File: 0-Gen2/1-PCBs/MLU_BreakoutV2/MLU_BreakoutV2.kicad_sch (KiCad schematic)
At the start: 41 parts, among them J1 Conn_02x24_Odd_Even, J10 Conn_01x17_Pin, J11 430450228, J12 430450228, J13 430450228, J14 430450228, J15 430450228, J16 430450228, J2 Conn_01x03_Pin, J21 430450228, J22 430450228, J3 PixHawk PM02, J4 BUS1, J5 BUS2, J6 Conn_01x02_Pin, J7 Conn_02x02_Odd_Even, J8 UART, J9 Conn_01x09_Pin, U1 MCP23008-E_P, U2 MCP9808_MSOP, U3 BME280, U4 Teensy4.1, U5 MCP9808_MSOP

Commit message: [add] MLU2 progress, [bugfix] depth sensor
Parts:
- removed J12, J13, J14, J15, J16, J21, J22: 430450228, ImportedV2:CONN_SD-43045-010_02_MOL, symbol Imported:430450228
- removed J6: Conn_01x02_Pin, Connector_PinHeader_2.54mm:PinHeader_1x02_P2.54mm_Vertical, symbol Connector:Conn_01x02_Pin
- removed J7: Conn_02x02_Odd_Even, Connector_PinHeader_2.54mm:PinHeader_2x02_P2.54mm_Vertical, symbol Connector_Generic:Conn_02x02_Odd_Even
- removed J9: Conn_01x09_Pin, Connector_PinHeader_2.54mm:PinHeader_1x09_P2.54mm_Vertical, symbol Connector:Conn_01x09_Pin
- removed JP1, JP2: Jumper_3_Bridged12, Jumper:SolderJumper-3_P1.3mm_Bridged2Bar12_RoundedPad1.0x1.5mm, symbol Jumper:Jumper_3_Bridged12
- added C5: 10uF, Capacitor_SMD:C_0805_2012Metric_Pad1.18x1.45mm_HandSolder, symbol Device:C
- added C6: 0.1uF, ImportedV2:K104K15X7RF5TL2_VIS, symbol Device:C
- added D1, D2: LED, LED_THT:LED_D3.0mm, symbol Device:LED
- added D3: 1N5817, Diode_THT:D_5W_P12.70mm_Horizontal, symbol Device:D
- added H10: Molex Socket Crimps, symbol Mechanical:MountingHole
- added H11, H8: Molex 4 Pin Male, symbol Mechanical:MountingHole
- added H12: MountingHole, MountingHole:MountingHole_3.2mm_M3, symbol Mechanical:MountingHole
- added H2, H5: IDC Cable, symbol Mechanical:MountingHole
- added H6: Socket for Teensy, symbol Mechanical:MountingHole
- added H7: Molex 10 Pin Male, symbol Mechanical:MountingHole
- added H9: Molex 2 Pin Male, symbol Mechanical:MountingHole
- added J12: J1B1211CCD, ImportedV2:J1B1211CCD, symbol Imported:J1B1211CCD
- added J13: Conn_02x03_Odd_Even, Connector_PinHeader_2.00mm:PinHeader_2x03_P2.00mm_Vertical, symbol Connector_Generic:Conn_02x03_Odd_Even
- added J14: 430451027, ImportedV2:CONN_SD-43045-010_10_MOL, symbol Imported:430451027
- added J17, J18, J19, J20, J23, J24: 430450228, ImportedV2:CONN_SD-43045-001_02_MOL, symbol Imported:430450228
- added J25, J7: SBH11-PBPC-D10-ST-BK, ImportedV2:SULLINS_SBH11-PBPC-D10-ST-BK, symbol Imported_Symbols:SBH11-PBPC-D10-ST-BK
- added J26: 430450422, ImportedV2:CONN_SD-43045-008_04_MOL, symbol Imported:430450422
- added J6, J9: 430450422, ImportedV2:CONN_SD-43045-009_04_MOL, symbol Imported:430450422
- added R8, R9: 140, Resistor_SMD:R_0805_2012Metric_Pad1.20x1.40mm_HandSolder, symbol Device:R_US
- added SW1: 09.03201.02, ImportedV2:09.03201_EAO, symbol Imported_Symbols:09.03201.02
- added U6: Teensy4.1, Module:Teensy41, symbol teensy:Teensy4.1
- added U8: BA033CC0FP-E2, ImportedV2:TO252-3_ROM, symbol Imported:BA033CC0FP-E2
- U3: footprint Imported Footprints:BME280 -> ImportedV2:BME280
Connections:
- net +3.3V: now also J19.2, J20.2, J25.18, J26.1, J7.18, U8.3 (OUT); no longer J1.11 (Pin_11), J1.15 (Pin_15), J1.23 (Pin_23)
- net +5V: now also J14.1, J17.1, J25.14, J25.16, J7.14, J7.16, J9.1, SW1.1, U8.1 (Vcc)
- net D5: now also J14.4
- net D6: now also J14.5
- net D7: now also J14.8
- net Dleak: now also U6.25 (33_MCLK2)
- net Dled1: now also J23.1, U6.29 (37_CS); no longer J1.3 (Pin_3)
- net Dled2: now also J24.1, U6.28 (36_CS); no longer J1.7 (Pin_7)
- net Dswitch1: now also J19.1, U6.18 (26_A12_MOSI1); no longer J1.9 (Pin_9)
- net Dswitch2: now also J20.1, J25.8, U6.19 (27_A13_SCK1); no longer J1.13 (Pin_13)
- net GND: now also C5.2, C6.1, J12.8 (GND), J12.9, J13.4 (Pin_4), J14.2, J18.2, J23.2, J24.2, J25.12, J25.20, J26.4, J7.12, J7.20, J9.4, R8.2, R9.2, U6.1 (GND), U6.34 (GND), U6.47 (GND), U6.64 (GND), U8.2 (GND); no longer J1.1 (Pin_1), J1.17 (Pin_17), J1.37 (Pin_37), J1.43 (Pin_43), J1.5 (Pin_5), J11.2
- net I2C1_SCL: now also J25.2, J26.3, J7.2, U6.41 (19_A5_SCL)
- net I2C1_SDA: now also J25.4, J26.2, J7.4, U6.40 (18_A4_SDA)
- net PWM0: now also J7.1, U6.2 (0_RX1_CRX2_CS1); no longer J11.1
- net PWM1: now also J7.3, U6.3 (1_TX1_CTX2_MISO1)
- net PWM2: now also J7.5, U6.4 (2_OUT2)
- net PWM3: now also J7.7, U6.5 (3_LRCLK2)
- net PWM4: now also J7.9, U6.6 (4_BCLK2)
- net PWM5: now also J7.11, U6.7 (5_IN2)
- net PWM6: now also J7.13, U6.8 (6_OUT1D)
- net PWM7: now also J7.15, U6.9 (7_RX2_OUT1A)
- net PWM8: no longer J1.47 (Pin_47)
- net SPI_CS1: now also J14.3
- net SPI_MISO: now also J14.9
- net SPI_MOSI: now also J14.6
- net SPI_SCK: now also J14.7
- net PWM9: no longer names the net of J1.41 (Pin_41)
- new net: C5.1, D2.2 (A), D3.2 (A), J17.2, SW1.3
- new net: C6.2, J12.2, J12.5
- new net: D1.2 (A), SW1.2
- new net: D1.1 (K), R8.1
- new net: D2.1 (K), R9.1
- new net LED: J12.10, J13.3 (Pin_3), U6.61 (LED)
- new net Lumen_PWM: J18.1, U6.10 (8_TX2_IN1)
- new net R+: J12.4, J13.1 (Pin_1), U6.60 (R+)
- new net R-: J12.6, J13.2 (Pin_2), U6.65 (R-)
- new net T+: J12.1, J13.6 (Pin_6), U6.63 (T+)
- new net T-: J12.3, J13.5 (Pin_5), U6.62 (T-)
- new net Teensy_5V: D3.1 (K), U6.48 (VIN)
- new net outNEO_CTRL_ESCs: J9.2
- new net outNEO_CTRL_ESCs_M: J7.8
- new net outNEO_CTRL_ESCs_S: J7.19
- new net toNEO_CTRL_ESCs_M: J7.6, U6.11 (9_OUT1C)
- new net toNEO_CTRL_ESCs_S: J7.17, U6.12 (10_CS_MQSR)
- new net toNEO_CTRL_EXTs: J9.3, U6.13 (11_MOSI_CTX1)
- no-connect marks 24 -> 44
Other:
- added sheet NEOs (NEOs.kicad_sch)
- note added: "-Route with diff pairs -Avoid vias"
- note added: "3.3V, 1A output"
- note added: "5V --> 3.3V Reg"
- note added: "Attach jumper when running off of 12V supply. Remove jumper when programming. -Expect 600mA draw"
- note added: "BlueRobotics Depth Sensor I2C @ 0x76"
- note added: "Bulkhead LEDs"
- note added: "Data Log Switch"
- note added: "Ethernet Breakout"
- note added: "Hardware/Software Kill Switch"
- note added: "Interconnect to ESC Board"
- note added: "Interconnect to Orin"
- note added: "Lumen LED PWM"
- note added: "Make sure to cut the 5V trace (or add diode): https://www.pjrc.com/teensy/external_power.html"
- note added: "More info: https://oshpark.com/shared_projects/wUFt1emZ https://www.pjrc.com/store/ethernet_kit.html"
- note added: "Neo_Interface_Exts"
- note added: "Neos"
- note added: "TODO: neopixel lines to power dist board Fix the screen pins"
- note added: "Teensy Reset Switch (Internal and External)"
- note added: "This is passed to Orin board"
- note added: "To external BlueRobotics switch on bulkhead"
- note added: "Vertical Mount"
- note added: "Vf=~2.2V, 20mA. Make this Green"
- note added: "Vf=~2.2V, 20mA. Make this Red"
- note added: "don't change pinout here"
- note added: "pick whether to chain from ESC board or have on new pin"
- note added: "socket here + leave space to mount"
- note removed: "0x76"
- note removed: "Bulkhead Interface"
- note removed: "Depth Sensor"
- note removed: "LEDs"
- note removed: "Lights Daisy Chain"
- note removed: "Note: light power supply must come from unregulated high voltage line"
- note removed: "Orin Passthrough"
- note removed: "Peripheral Interfaces"
- note removed: "Power Distrbution Interface"
- note removed: "Thruster Interface"
- note removed: "Towards the bulkhead"
- note removed: "likely move these to the ESC board"
- moved on the sheet: C1, C2, C3, J3, J8, JP3, R6, R7, RN1A, RN1B, RN1C, RN1D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

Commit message: [bugfix] depth via BME 0x76 removal, [add] MLUv2 progress
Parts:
- removed C1, C2: 135p, Capacitor_SMD:C_0603_1608Metric_Pad1.08x0.95mm_HandSolder, symbol Device:C
- removed C3, C4: 10uF, Capacitor_SMD:C_0805_2012Metric_Pad1.18x1.45mm_HandSolder, symbol Device:C
- removed H8: Molex 4 Pin Male, symbol Mechanical:MountingHole
- removed J1: Conn_02x24_Odd_Even, Connector_PinSocket_2.54mm:PinSocket_2x24_P2.54mm_Horizontal, symbol Connector_Generic:Conn_02x24_Odd_Even
- removed J18, J19, J20, J23, J24: 430450228, ImportedV2:CONN_SD-43045-001_02_MOL, symbol Imported:430450228
- removed J2: Conn_01x03_Pin, Connector_PinHeader_2.54mm:PinHeader_1x03_P2.54mm_Vertical, symbol Connector:Conn_01x03_Pin
- removed J26: 430450422, ImportedV2:CONN_SD-43045-008_04_MOL, symbol Imported:430450422
- removed J4: BUS1, Connector_PinSocket_2.54mm:PinSocket_1x04_P2.54mm_Vertical, symbol Connector:Conn_01x04_Pin
- removed J5: BUS2, Connector_PinSocket_2.54mm:PinSocket_1x04_P2.54mm_Vertical, symbol Connector:Conn_01x04_Pin
- removed JP3: Jumper_3_Bridged12, Jumper:SolderJumper-3_P1.3mm_Bridged2Bar12_RoundedPad1.0x1.5mm, symbol Jumper:Jumper_3_Bridged12
- removed R1, R2, R3, R6, R7: 10k, Resistor_SMD:R_0805_2012Metric_Pad1.20x1.40mm_HandSolder, symbol Device:R_US
- removed RN1: 10kΩ, Resistor_SMD:R_Array_Convex_4x0612, symbol Lab_3:R_Pack04_Split
- removed U1: MCP23008-E_P, Imported Footprints:MCP3008, symbol Imported:MCP23008-E_P
- removed U2, U5: MCP9808_MSOP, Package_SO:MSOP-8_3x3mm_P0.65mm, symbol Sensor_Temperature:MCP9808_MSOP
- removed U3: BME280, ImportedV2:BME280, symbol Sensor:BME280
- added J8: Conn_02x20_Odd_Even, Connector_PinSocket_2.54mm:PinSocket_2x20_P2.54mm_Vertical, symbol Connector_Generic:Conn_02x20_Odd_Even
- added JP4, JP7: Jumper_2_Small_Open, Jumper:SolderJumper-2_P1.3mm_Open_RoundedPad1.0x1.5mm, symbol Jumper:Jumper_2_Small_Open
- added JP5, JP6: Jumper_2_Small_Bridged, Jumper:SolderJumper-2_P1.3mm_Bridged2Bar_RoundedPad1.0x1.5mm, symbol Jumper:Jumper_2_Small_Bridged
- renumbered C5 to C1, C6 to C2, D3 to D1, D1 to D2, D2 to D3, H11 to H1, H3 to H10, H4 to H11, H7 to H2, H9 to H3, H10 to H4, H2 to H5, H5 to H7, H1 to H8, H12 to H9, J12 to J10, J13 to J11, J3 to J12, J25 to J13, J6 to J14, J11 to J15, J8 to J16, J9 to J4, J14 to J5, J17 to J6, J10 to J9, R8 to R6, R9 to R7, U4 to U1, U8 to U5
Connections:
- net +3.3V: now also J13.7, J8.19 (Pin_19), J8.3 (Pin_3); no longer J13.18, U1.15 (3V3), U1.46 (3V3)
- net +5V: now also J13.1, J13.3, J13.5, J4.4, J8.1 (Pin_1), J8.17 (Pin_17); no longer J13.14, J13.16, J4.1, U1.48 (VIN)
- net Ab_s: no longer U1.44 (22_A8_CTX1)
- net Ai_s: no longer U1.45 (23_A9_CRX1_MCLK1)
- net Analog_Current: now also U6.33 (41_A17), JP4.1 (A), JP5.2 (B); no longer U1.33 (41_A17)
- net Analog_Voltage: now also U6.32 (40_A16), JP6.2 (B), JP7.2 (B); no longer U1.32 (40_A16)
- net D5: no longer U1.36 (14_A0_TX3_SPDIF_OUT)
- net Dleak: no longer U1.25 (33_MCLK2)
- net Dled1: no longer U1.29 (37_CS)
- net Dled2: no longer U1.28 (36_CS)
- net Dswitch1: no longer U1.18 (26_A12_MOSI1)
- net Dswitch2: now also J13.6; no longer J13.8, U1.19 (27_A13_SCK1)
- net GND: now also J13.13, J13.15, J13.17, J13.19, J4.2, J8.18 (Pin_18), J8.2 (Pin_2), J8.20 (Pin_20), J8.34 (Pin_34), J8.36 (Pin_36), J8.4 (Pin_4), JP4.2 (B), JP7.1 (A); no longer J13.12, J13.20, J4.4, U1.1 (GND), U1.34 (GND), U1.47 (GND)
- net I2C1_SCL: now also J8.7 (Pin_7); no longer U1.41 (19_A5_SCL)
- net I2C1_SDA: now also J8.5 (Pin_5); no longer U1.40 (18_A4_SDA)
- net I2C2_SCL: now also U6.38 (16_A2_RX4_SCL1), J8.8 (Pin_8); no longer U1.38 (16_A2_RX4_SCL1)
- net I2C2_SDA: now also U6.39 (17_A3_TX4_SDA1), J8.6 (Pin_6); no longer U1.39 (17_A3_TX4_SDA1)
- net PWM0: no longer U1.2 (0_RX1_CRX2_CS1)
- net PWM1: no longer U1.3 (1_TX1_CTX2_MISO1)
- net PWM2: no longer U1.4 (2_OUT2)
- net PWM3: no longer U1.5 (3_LRCLK2)
- net PWM4: no longer U1.6 (4_BCLK2)
- net PWM5: no longer U1.7 (5_IN2)
- net PWM6: no longer U1.8 (6_OUT1D)
- net PWM7: no longer U1.9 (7_RX2_OUT1A)
- net SPI_CS1: now also U6.12 (10_CS_MQSR); no longer U1.12 (10_CS_MQSR)
- net SPI_MISO: now also U6.14 (12_MISO_MQSL); no longer U1.14 (12_MISO_MQSL)
- net SPI_MOSI: now also U6.13 (11_MOSI_CTX1); no longer U1.13 (11_MOSI_CTX1)
- net SPI_SCK: now also U6.35 (13_SCK_LED); no longer U1.35 (13_SCK_LED)
- net UART_RX2: now also U6.20 (28_RX7), J8.26 (Pin_26); no longer U1.20 (28_RX7)
- net UART_RX3: now also U6.17 (25_A11_RX6_SDA2), J8.30 (Pin_30)
- net UART_TX2: now also U6.21 (29_TX7), J8.28 (Pin_28); no longer U1.21 (29_TX7)
- net UART_TX3: now also U6.16 (24_A10_TX6_SCL2), J8.32 (Pin_32)
- net outNEO_CTRL_ESCs: now also J4.1; no longer J4.2
- net toNEO_CTRL_ESCs_M: no longer U6.11 (9_OUT1C)
- net toNEO_CTRL_ESCs_S: no longer U6.12 (10_CS_MQSR)
- net toNEO_CTRL_EXTs: no longer U6.13 (11_MOSI_CTX1)
- net D/A14: now reaches U6.36 (14_A0_TX3_SPDIF_OUT)
- net D/A14: now also J8.10 (Pin_10)
- net GPIOExp_INT: now reaches U6.37 (15_A1_RX3_SPDIF_IN)
- net D/A20: now reaches U6.42 (20_A6_TX5_LRCLK1)
- net D/A20: now also J8.9 (Pin_9)
- net D/A21: now reaches U6.43 (21_A7_RX5_BCLK1)
- net D/A21: now also J8.11 (Pin_11)
- net D/A22: now reaches U6.44 (22_A8_CTX1)
- net D/A22: now also J8.13 (Pin_13)
- net D/A23: now reaches U6.45 (23_A9_CRX1_MCLK1)
- net D/A23: now also J8.15 (Pin_15)
- net Host_D-: now reaches U6.56 (D-)
- net Host_D-: now also J8.21 (Pin_21)
- net Host_D+: now reaches U6.57 (D+)
- net Host_D+: now also J8.23 (Pin_23)
- net at J13.10: now also JP6.1 (A)
- net A3: no longer names the net of U1.43 (21_A7_RX5_BCLK1)
- net A4: no longer names the net of U1.42 (20_A6_TX5_LRCLK1)
- net Dint: no longer names the net of U1.37 (15_A1_RX3_SPDIF_IN)
- net PWM8: no longer names the net of U1.10 (8_TX2_IN1)
- new net: J13.8, JP5.1 (A)
- no-connect marks 44 -> 38
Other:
- sheet NEOs renamed Neopixels
- added sheet GPIO_Expander (GPIO_Expander.kicad_sch)
- added sheet On-board Sensors (sensors.kicad_sch)
- added sheet Peripheral Connectors (peripherals.kicad_sch)
- sheet Neopixels ports: added outNEO_MLU, toNEO_MLU; removed none
- note added: "5V Orin-->MLU 3.3V MLU-->Orin"
- note added: "Arm Host"
- note added: "Extra Pin Breakout"
- note added: "Interrupt to GPIO Expander"
- note added: "Secondary I2C Bus"
- note added: "Solder resistors onto jumpers if voltage division is necessary"
- note added: "TODO: neopixel lines to power dist board fix the screen pins subset LEDs on MLU arm connector XT30s for 12V? Smaller ribbon for Orin interface"
- note added: "optional pull-ups"
- note removed: "Analog Inputs"
- note removed: "Analog Inputs Sonar Localization"
- note removed: "Attach jumper when running off of 12V supply. Remove jumper when programming. -Expect 600mA draw"
- note removed: "Battery sampling"
- note removed: "BlueRobotics Depth Sensor I2C @ 0x76"
- note removed: "Bulkhead LEDs"
- note removed: "CTD Comms"
- note removed: "Center leak detector to be mounted on lower board"
- note removed: "Data Log Switch"
- note removed: "Downstream pull-up"
- note removed: "EXT LED"
- note removed: "For Sonar"
- note removed: "GPIO Expander"
- note removed: "Hardware/Software Kill Switch"
- note removed: "I2C @ 0x18 format: 0011(A2)(A1)(A0)"
- note removed: "I2C @ 0x19 format: 0011(A2)(A1)(A0)"
- note removed: "I2C @ 0x20 format: 0100(A2)(A1)(A0)"
- note removed: "I2C @ 0x76 when SDO low I2C @ 0x77 when SDO high"
- note removed: "Integrated BME280"
- note removed: "Integrated MCP9808 #1"
- note removed: "Integrated MCP9808 #2"
- note removed: "Lumen LED PWM"
- note removed: "Orin/IMU Temp"
- note removed: "TODO: neopixel lines to power dist board Fix the screen pins"
- note removed: "This is passed to Orin board"
- note removed: "socket here + leave space to mount"
- company: (none) -> Stanford Robosub
- title: (none) -> Main Logic Unit Breakout
- moved on the sheet: H10, H11, H7, H8, H9, J12, J13, J14, J15, J16, J9, U1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

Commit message: [changes] MLUv2
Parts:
- removed C1: 10uF, Capacitor_SMD:C_0805_2012Metric_Pad1.18x1.45mm_HandSolder, symbol Device:C
- removed C2: 0.1uF, ImportedV2:K104K15X7RF5TL2_VIS, symbol Device:C
- removed D1: 1N5817, Diode_THT:D_5W_P12.70mm_Horizontal, symbol Device:D
- removed D2, D3: LED, LED_THT:LED_D3.0mm, symbol Device:LED
- removed H1: Molex 4 Pin Male, symbol Mechanical:MountingHole
- removed H2: Molex 10 Pin Male, symbol Mechanical:MountingHole
- removed H3: Molex 2 Pin Male, symbol Mechanical:MountingHole
- removed H4: Molex Socket Crimps, symbol Mechanical:MountingHole
- removed H6: Socket for Teensy, symbol Mechanical:MountingHole
- removed J10: J1B1211CCD, ImportedV2:J1B1211CCD, symbol Imported:J1B1211CCD
- removed J11: Conn_02x03_Odd_Even, Connector_PinHeader_2.00mm:PinHeader_2x03_P2.00mm_Vertical, symbol Connector_Generic:Conn_02x03_Odd_Even
- removed J12: PixHawk PM02, Connector_PinSocket_2.54mm:PinSocket_1x06_P2.54mm_Vertical, symbol Connector:Conn_01x06_Pin
- removed J14, J4: 430450422, ImportedV2:CONN_SD-43045-009_04_MOL, symbol Imported:430450422
- removed J15: 430450228, ImportedV2:CONN_SD-43045-010_02_MOL, symbol Imported:430450228
- removed J16: UART, Connector_PinSocket_2.54mm:PinSocket_1x02_P2.54mm_Vertical, symbol Connector:Conn_01x02_Pin
- removed J5: 430451027, ImportedV2:CONN_SD-43045-010_10_MOL, symbol Imported:430451027
- removed J6: 430450228, ImportedV2:CONN_SD-43045-001_02_MOL, symbol Imported:430450228
- removed J8: Conn_02x20_Odd_Even, Connector_PinSocket_2.54mm:PinSocket_2x20_P2.54mm_Vertical, symbol Connector_Generic:Conn_02x20_Odd_Even
- removed J9: Conn_01x17_Pin, Connector_PinHeader_2.54mm:PinHeader_1x17_P2.54mm_Horizontal, symbol Connector:Conn_01x17_Pin
- removed R6, R7: 140, Resistor_SMD:R_0805_2012Metric_Pad1.20x1.40mm_HandSolder, symbol Device:R_US
- removed SW1: 09.03201.02, ImportedV2:09.03201_EAO, symbol Imported_Symbols:09.03201.02
- removed U1: Teensy4.1, Module:Teensy41, symbol teensy:Teensy4.1
- removed U5: BA033CC0FP-E2, ImportedV2:TO252-3_ROM, symbol Imported:BA033CC0FP-E2
- added JP61, JP62, JP63, JP64, JP65, JP66: Jumper_2_Small_Open, Jumper:SolderJumper-2_P1.3mm_Open_RoundedPad1.0x1.5mm, symbol Jumper:Jumper_2_Small_Open
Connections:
- net Dleak is gone; now on net toNEO_CTRL_Orin: U6.25 (33_MCLK2)
- net outNEO_CTRL_ESCs_M is gone; now on net outNEO_CTRL_ESCs: J7.8
- net toNEO_CTRL_ESCs_M is gone; now on net toNEO_CTRL_ESCs: J7.6
- net +3.3V: no longer J13.7
- net +5V: now also J13.7
- net D/A20: now also JP64.2 (B)
- net D/A21: now also JP63.2 (B)
- net D/A22: now also JP62.2 (B)
- net D/A23: now also JP61.2 (B)
- net UART_RX1: now also U6.26 (34_RX8)
- net UART_TX1: now also U6.27 (35_TX8)
- net toNEO_CTRL_EXTs: now also U6.30 (38_CS1_IN1)
- net toNEO_CTRL_MLU: now also U6.31 (39_MISO1_OUT1A)
- net toNEO_CTRL_ESCs: now reaches U6.11 (9_OUT1C)
- net DISP_RST: now reaches U6.22 (30_CRX3)
- net DISP_DC: now reaches U6.23 (31_CTX3)
- net DISP_LED: now reaches U6.24 (32_OUT1B)
- net Device_D-: now reaches U6.66 (D-)
- net Device_D-: now also JP66.1 (A)
- net Device_D+: now reaches U6.67 (D+)
- net Device_D+: now also JP65.1 (A)
- net at J13.11: now also JP65.2 (B)
- net at J13.12: now also JP61.1 (A)
- net at J13.14: now also JP62.1 (A)
- net at J13.16: now also JP63.1 (A)
- net at J13.18: now also JP64.1 (A)
- net toNEO_CTRL_Orin: now reaches J13.20
- net at J13.9: now also JP66.2 (B)
- net outNEO_CTRL_ESCs_S: no longer names the net of J7.19
- net toNEO_CTRL_ESCs_S: no longer names the net of J7.17
- no-connect marks 38 -> 14
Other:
- added sheet Power Management (Power_management.kicad_sch)
- sheet On-board Sensors ports: added I2C1_SCL, I2C1_SDA; removed none
- note added: "5V Orin-->MLU Orin requires own 5V --> 3.3V converter"
- note added: "Orin Interconnects"
- note added: "TODO: Smaller ribbon for Orin interface"
- note added: "Teensy Device"
- note removed: "-Route with diff pairs -Avoid vias"
- note removed: "2.2" TFT Screen"
- note removed: "3.3V, 1A output"
- note removed: "5V --> 3.3V Reg"
- note removed: "5V Orin-->MLU 3.3V MLU-->Orin"
- note removed: "Arm"
- note removed: "Ethernet Breakout"
- note removed: "Extra I2C"
- note removed: "Extra Pin Breakout"
- note removed: "FET Temp"
- note removed: "Intermediate Signals"
- note removed: "Interrupts"
- note removed: "Low Speed"
- note removed: "Make sure to cut the 5V trace (or add diode): https://www.pjrc.com/teensy/external_power.html"
- note removed: "More info: https://oshpark.com/shared_projects/wUFt1emZ https://www.pjrc.com/store/ethernet_kit.html"
- note removed: "Neo_Interface_Exts"
- note removed: "Power"
- note removed: "Power In"
- note removed: "Power Management"
- note removed: "Power Management Interface"
- note removed: "Sampling"
- note removed: "TODO: neopixel lines to power dist board fix the screen pins subset LEDs on MLU arm connector XT30s for 12V? Smaller ribbon for Orin interface"
- note removed: "Teensy Reset Switch (Internal and External)"
- note removed: "To external BlueRobotics switch on bulkhead"
- note removed: "UART Main"
- note removed: "Vertical Mount"
- note removed: "Vf=~2.2V, 20mA. Make this Green"
- note removed: "Vf=~2.2V, 20mA. Make this Red"
- note removed: "pick whether to chain from ESC board or have on new pin"
- moved on the sheet: H10, H11, H5, H7, H8, H9, J13, J7, JP4, JP5, JP6, JP7

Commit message: [final pass] MLU breakout
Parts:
- removed H10, H11, H8, H9: MountingHole, MountingHole:MountingHole_3.2mm_M3, symbol Mechanical:MountingHole
- removed JP61, JP62, JP63, JP64, JP65, JP66: Jumper_2_Small_Open, Jumper:SolderJumper-2_P1.3mm_Open_RoundedPad1.0x1.5mm, symbol Jumper:Jumper_2_Small_Open
- added JP41, JP49, JP50, JP51, JP52, JP53: Jumper_2_Small_Open, Connector_PinHeader_1.27mm:PinHeader_1x02_P1.27mm_Vertical, symbol Jumper:Jumper_2_Small_Open
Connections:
- net Device_D+: now also JP41.1 (A)
- net Device_D-: now also JP49.1 (A)
- net D/A20: now also JP53.1 (A)
- net D/A21: now also JP52.1 (A)
- net D/A22: now also JP51.1 (A)
- net D/A23: now also JP50.1 (A)
- net GND: no longer U6.64 (GND)
- net at J13.12: now also JP50.2 (B)
- net at J13.18: now also JP53.2 (B)
- net at J13.11: now also JP41.2 (B)
- net at J13.14: now also JP51.2 (B)
- net at J13.16: now also JP52.2 (B)
- net at J13.9: now also JP49.2 (B)
- new net ETH_GND: U6.64 (GND)

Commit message: almost done with all orders
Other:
- note removed: "TODO: Smaller ribbon for Orin interface"
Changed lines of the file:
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@@
-		)
-	)
-	(text "TODO: \nSmaller ribbon for Orin interface"
-		(exclude_from_sim no)
-		(at 116.586 93.218 0)
-		(effects
-			(font
-				(size 2.032 2.032)
-			)
-			(justify left)
 		)
 	)

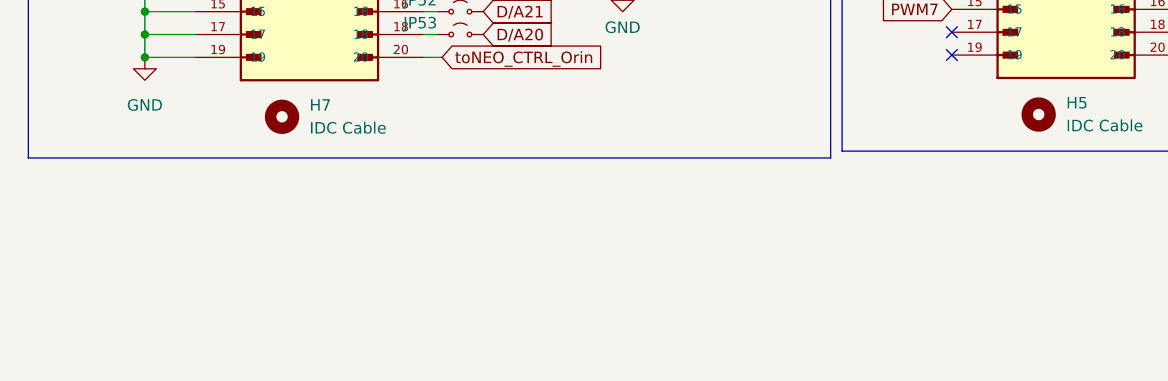
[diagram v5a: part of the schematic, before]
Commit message: [bugfixing] board bringup
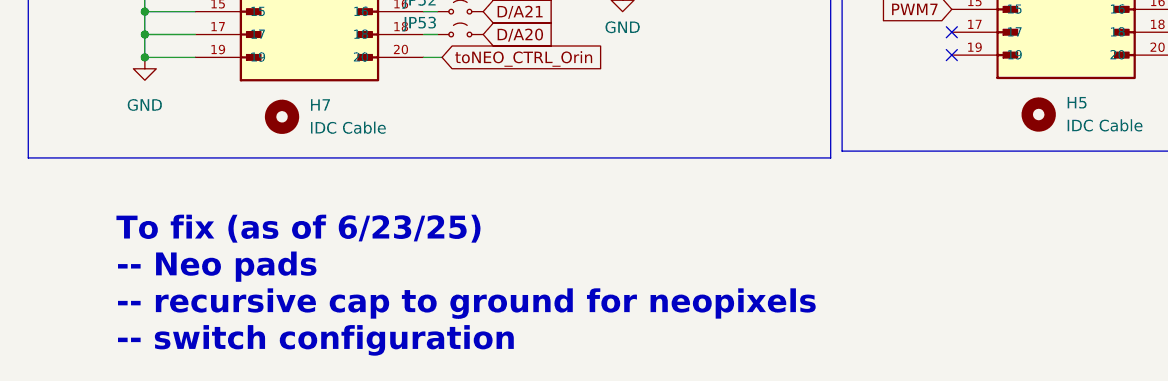
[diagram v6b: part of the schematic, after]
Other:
- note added: "To fix (as of 6/23/25) -- Neo pads -- recursive cap to ground for neopixels -- switch configuration"
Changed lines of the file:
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@@
+		)
+	)
+	(text "To fix (as of 6/23/25)\n-- Neo pads\n-- recursive cap to ground for neopixels\n-- switch configuration"
+		(exclude_from_sim no)
+		(at 24.765 176.2125 0)
+		(effects
+			(font
+				(size 2.54 2.54)
+				(thickness 0.508)
+				(bold yes)
+				(color 132 0 0 1)
+			)
+			(justify left)
 		)
 	)

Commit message: pushing after comp
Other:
- note added: "To fix (as of 8/16/25) -- Neo pads -- recursive cap to ground for neopixels -- switch configuration -- pin 38 needs to be changed (hard coded to SD card so no neos)"
- note removed: "To fix (as of 6/23/25) -- Neo pads -- recursive cap to ground for neopixels -- switch configuration"
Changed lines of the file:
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@@
 		)
 	)
-	(text "To fix (as of 6/23/25)\n-- Neo pads\n-- recursive cap to ground for neopixels\n-- switch configuration"
+	(text "To fix (as of 8/16/25)\n-- Neo pads\n-- recursive cap to ground for neopixels\n-- switch configuration\n-- pin 38 needs to be changed (hard coded to SD card so no neos)"
 		(exclude_from_sim no)
 		(at 24.765 176.2125 0)
